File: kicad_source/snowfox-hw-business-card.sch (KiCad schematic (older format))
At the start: 7 parts, among them CN2 CONN_01X18, CN3 CONN_01X18

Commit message: added flash, JTAG connector and display to schematic
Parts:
- removed CN2, CN3: CONN_01X18, pin_headers:Pin_Header_Straight_1x18, symbol mechanical-connectors:CONN_01X18
- removed D1: 150060YS75000, LEDs:LED_0603, symbol devices:Led_Small
- removed R1: 3k3, resistors:R_0603, symbol devices:R_0603
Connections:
- net labels removed: +3V3, GND, PEX_PIN1, PEX_PIN10, PEX_PIN11, PEX_PIN12, PEX_PIN13, PEX_PIN14, PEX_PIN16, PEX_PIN20, PEX_PIN23, PEX_PIN25, PEX_PIN28, PEX_PIN3, PEX_PIN30, PEX_PIN31, PEX_PIN32, PEX_PIN33, PEX_PIN42, PEX_PIN44, PEX_PIN45, PEX_PIN46, PEX_PIN47, PEX_PIN48, PEX_PIN49, PEX_PIN5, PEX_PIN51, PEX_PIN6, PEX_PIN7, PEX_PIN8, PEX_RST, WM_PIO24, WM_PIO25
- wire segments 45 -> 0

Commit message: added nfc part, generated schematic pdf
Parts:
- renumbered MECH3 to MECH1, MECH4 to MECH2, MECH5 to MECH3
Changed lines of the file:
@@
 $Descr A4 11693 8268
 encoding utf-8
-Sheet 1 6
+Sheet 1 7
 Title "snowfox-hw-business-card"
-Date "2020-05-07"
+Date "2020-05-10"
 Rev "dev_0.1"
 Comp "generationmake"
@@
 $EndDescr
 $Comp
-L MECH_mounting-holes:MHP_3.2_5.8 MECH3
+L MECH_mounting-holes:MHP_3.2_5.8 MECH1
 U 1 1 5E401602
 P 1000 7600
-F 0 "MECH3" H 1128 7646 50  0000 L CNN
+F 0 "MECH1" H 1128 7646 50  0000 L CNN
 F 1 "MHP_3.2_5.8" H 1128 7555 50  0000 L CNN
 F 2 "MECH_mounting_holes:MHP_3.2_5.8" H 900 7650 50  0001 C CNN
@@
 $EndComp
 $Comp
-L MECH_mounting-holes:MHP_3.2_5.8 MECH4
+L MECH_mounting-holes:MHP_3.2_5.8 MECH2
 U 1 1 5E401D77
 P 2000 7600
-F 0 "MECH4" H 2128 7646 50  0000 L CNN
+F 0 "MECH2" H 2128 7646 50  0000 L CNN
 F 1 "MHP_3.2_5.8" H 2128 7555 50  0000 L CNN
 F 2 "MECH_mounting_holes:MHP_3.2_5.8" H 1900 7650 50  0001 C CNN
@@
 $EndComp
 $Comp
-L MECH_mounting-holes:MHP_3.2_5.8 MECH5
+L MECH_mounting-holes:MHP_3.2_5.8 MECH3
 U 1 1 5E402150
 P 3000 7600
-F 0 "MECH5" H 3128 7646 50  0000 L CNN
+F 0 "MECH3" H 3128 7646 50  0000 L CNN
 F 1 "MHP_3.2_5.8" H 3128 7555 50  0000 L CNN
 F 2 "MECH_mounting_holes:MHP_3.2_5.8" H 2900 7650 50  0001 C CNN
@@
 F1 "history.sch" 43
 $EndSheet
+$Sheet
+S 3000 2000 1000 500
+U 5EB7BA95
+F0 "NFC" 43
+F1 "nfc.sch" 43
+$EndSheet
 $EndSCHEMATC

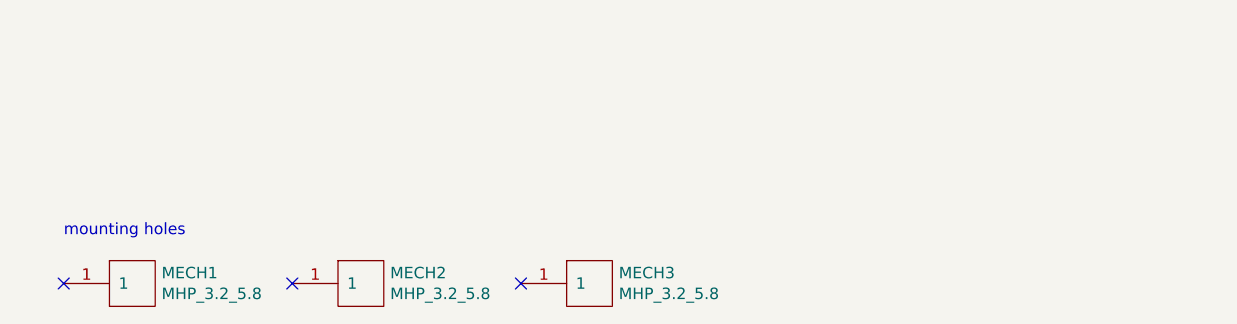
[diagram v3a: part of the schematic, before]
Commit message: used small side switch for reset, added expansion connector,changed mounting holes
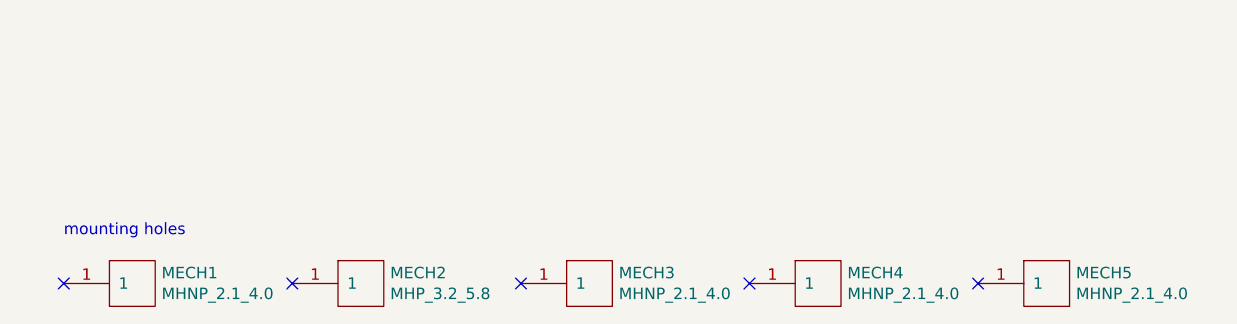
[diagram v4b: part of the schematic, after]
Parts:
- removed MECH1, MECH3: MHP_3.2_5.8, MECH_mounting_holes:MHP_3.2_5.8, symbol MECH_mounting-holes:MHP_3.2_5.8
- added MECH1, MECH3, MECH4, MECH5: MHNP_2.1_4.0, MECH_mounting_holes:MH_210_400_NP, symbol MECH_mounting-holes:MHNP_2.1_4.0
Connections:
- no-connect marks 3 -> 5
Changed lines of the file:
@@
 Comment4 ""
 $EndDescr
-$Comp
-L MECH_mounting-holes:MHP_3.2_5.8 MECH1
-U 1 1 5E401602
-P 1000 7600
-F 0 "MECH1" H 1128 7646 50  0000 L CNN
-F 1 "MHP_3.2_5.8" H 1128 7555 50  0000 L CNN
-F 2 "MECH_mounting_holes:MHP_3.2_5.8" H 900 7650 50  0001 C CNN
-F 3 "" H 1000 7600 50  0001 C CNN
-	1    1000 7600
-	1    0    0    -1
-$EndComp
-$Comp
-L MECH_mounting-holes:MHP_3.2_5.8 MECH2
-U 1 1 5E401D77
-P 2000 7600
-F 0 "MECH2" H 2128 7646 50  0000 L CNN
-F 1 "MHP_3.2_5.8" H 2128 7555 50  0000 L CNN
-F 2 "MECH_mounting_holes:MHP_3.2_5.8" H 1900 7650 50  0001 C CNN
-F 3 "" H 2000 7600 50  0001 C CNN
-	1    2000 7600
-	1    0    0    -1
-$EndComp
-$Comp
-L MECH_mounting-holes:MHP_3.2_5.8 MECH3
-U 1 1 5E402150
-P 3000 7600
-F 0 "MECH3" H 3128 7646 50  0000 L CNN
-F 1 "MHP_3.2_5.8" H 3128 7555 50  0000 L CNN
-F 2 "MECH_mounting_holes:MHP_3.2_5.8" H 2900 7650 50  0001 C CNN
-F 3 "" H 3000 7600 50  0001 C CNN
-	1    3000 7600
-	1    0    0    -1
-$EndComp
-NoConn ~ 2700 7600
 NoConn ~ 1700 7600
 NoConn ~ 700  7600
@@
 F1 "nfc.sch" 43
 $EndSheet
+$Comp
+L MECH_mounting-holes:MHP_3.2_5.8 MECH2
+U 1 1 5ED84539
+P 2000 7600
+F 0 "MECH2" H 2128 7646 50  0000 L CNN
+F 1 "MHP_3.2_5.8" H 2128 7555 50  0000 L CNN
+F 2 "MECH_mounting_holes:MHP_3.2_5.8" H 1900 7650 50  0001 C CNN
+F 3 "" H 2000 7600 50  0001 C CNN
+	1    2000 7600
+	1    0    0    -1
+$EndComp
+$Comp
+L MECH_mounting-holes:MHNP_2.1_4.0 MECH1
+U 1 1 5ED847C4
+P 1000 7600
+F 0 "MECH1" H 1128 7646 50  0000 L CNN
+F 1 "MHNP_2.1_4.0" H 1128 7555 50  0000 L CNN
+F 2 "MECH_mounting_holes:MH_210_400_NP" H 900 7650 50  0001 C CNN
+F 3 "" H 1000 7600 50  0001 C CNN
+	1    1000 7600
+	1    0    0    -1
+$EndComp
+NoConn ~ 2700 7600
+$Comp
+L MECH_mounting-holes:MHNP_2.1_4.0 MECH3
+U 1 1 5ED84C02
+P 3000 7600
+F 0 "MECH3" H 3128 7646 50  0000 L CNN
+F 1 "MHNP_2.1_4.0" H 3128 7555 50  0000 L CNN
+F 2 "MECH_mounting_holes:MH_210_400_NP" H 2900 7650 50  0001 C CNN
+F 3 "" H 3000 7600 50  0001 C CNN
+	1    3000 7600
+	1    0    0    -1
+$EndComp
+NoConn ~ 3700 7600
+$Comp
+L MECH_mounting-holes:MHNP_2.1_4.0 MECH4
+U 1 1 5ED85171
+P 4000 7600
+F 0 "MECH4" H 4128 7646 50  0000 L CNN
+F 1 "MHNP_2.1_4.0" H 4128 7555 50  0000 L CNN
+F 2 "MECH_mounting_holes:MH_210_400_NP" H 3900 7650 50  0001 C CNN
+F 3 "" H 4000 7600 50  0001 C CNN
+	1    4000 7600
+	1    0    0    -1
+$EndComp
+NoConn ~ 4700 7600
+$Comp
+L MECH_mounting-holes:MHNP_2.1_4.0 MECH5
+U 1 1 5ED85C08
+P 5000 7600
+F 0 "MECH5" H 5128 7646 50  0000 L CNN
+F 1 "MHNP_2.1_4.0" H 5128 7555 50  0000 L CNN
+F 2 "MECH_mounting_holes:MH_210_400_NP" H 4900 7650 50  0001 C CNN
+F 3 "" H 5000 7600 50  0001 C CNN
+	1    5000 7600
+	1    0    0    -1
+$EndComp
 $EndSCHEMATC

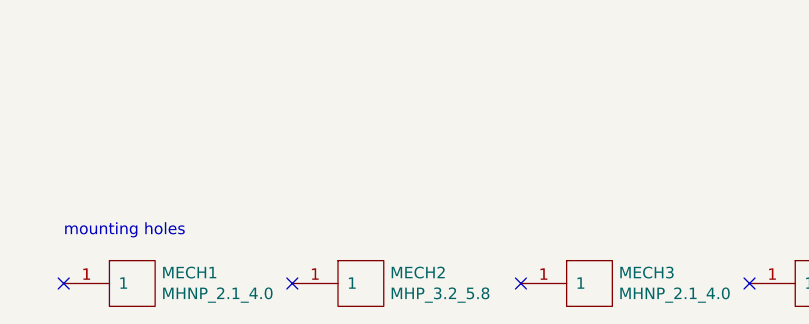
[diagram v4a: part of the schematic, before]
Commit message: rearranged parts for display
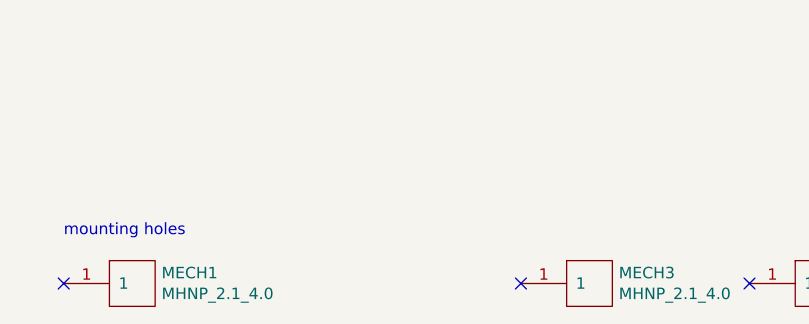
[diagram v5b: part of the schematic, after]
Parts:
- removed MECH2: MHP_3.2_5.8, MECH_mounting_holes:MHP_3.2_5.8, symbol MECH_mounting-holes:MHP_3.2_5.8
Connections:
- no-connect marks 5 -> 4
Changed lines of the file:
@@
 Comment4 ""
 $EndDescr
-NoConn ~ 1700 7600
 NoConn ~ 700  7600
 Text Notes 700  7400 0    50   ~ 0
@@
 $EndSheet
 $Comp
-L MECH_mounting-holes:MHP_3.2_5.8 MECH2
-U 1 1 5ED84539
-P 2000 7600
-F 0 "MECH2" H 2128 7646 50  0000 L CNN
-F 1 "MHP_3.2_5.8" H 2128 7555 50  0000 L CNN
-F 2 "MECH_mounting_holes:MHP_3.2_5.8" H 1900 7650 50  0001 C CNN
-F 3 "" H 2000 7600 50  0001 C CNN
-	1    2000 7600
-	1    0    0    -1
-$EndComp
-$Comp
 L MECH_mounting-holes:MHNP_2.1_4.0 MECH1

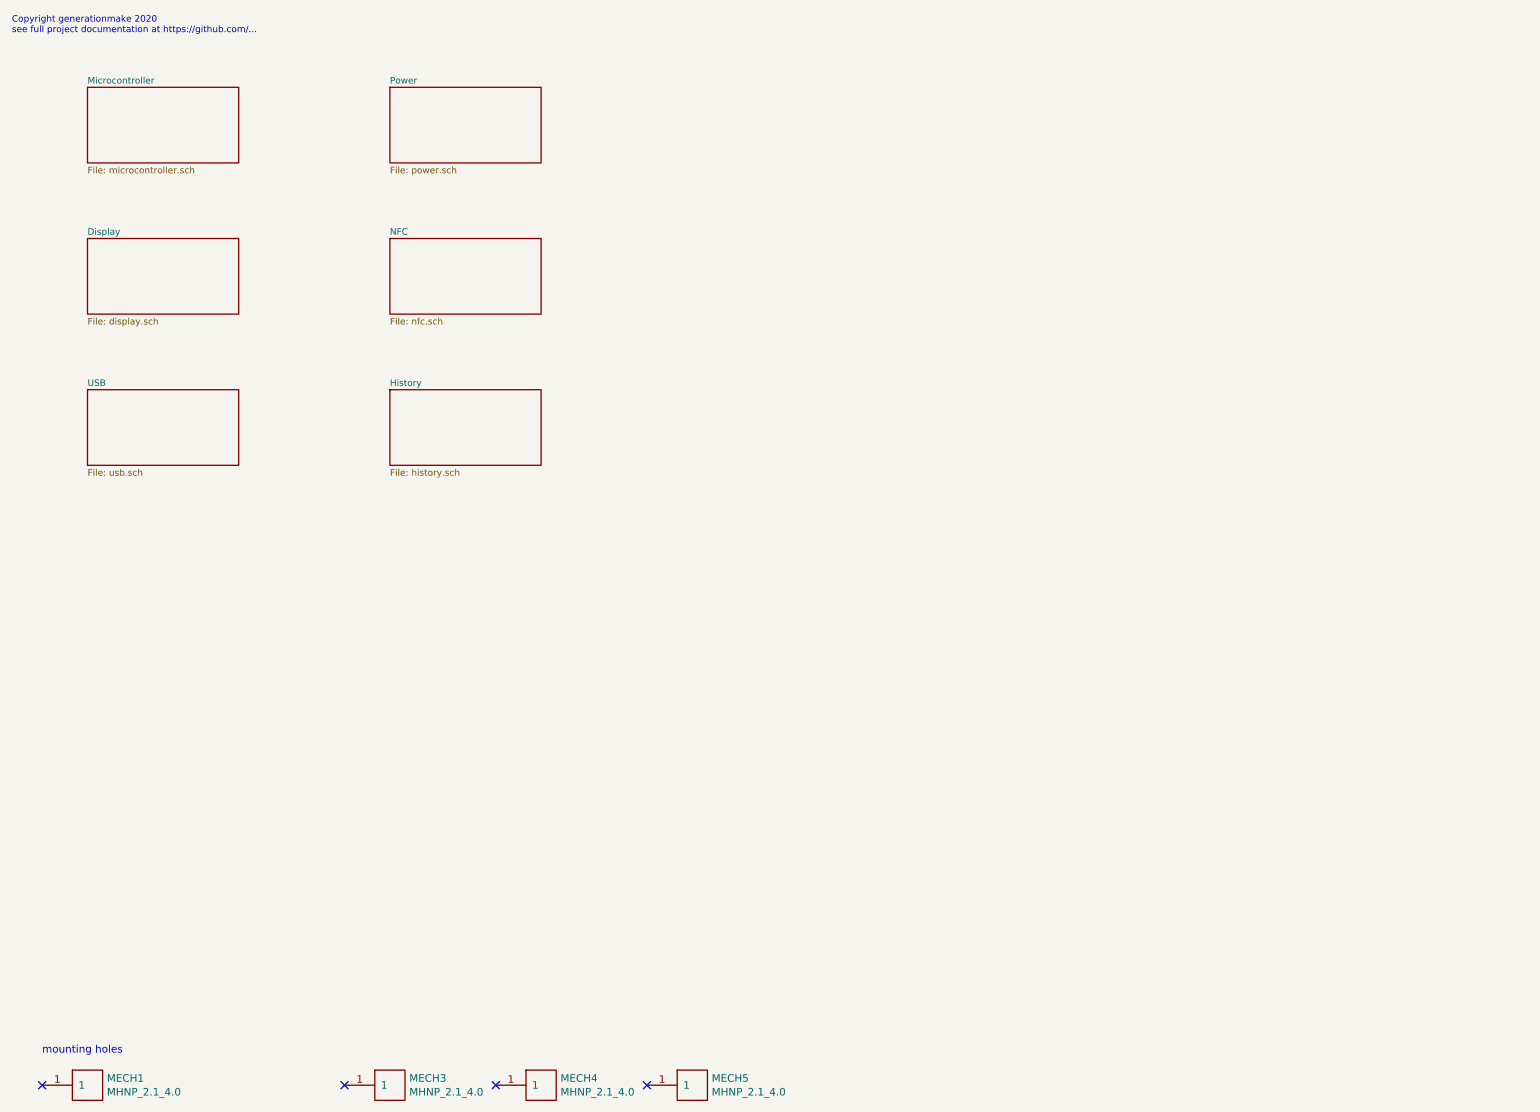
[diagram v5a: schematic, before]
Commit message: added C45 to pin4 of display
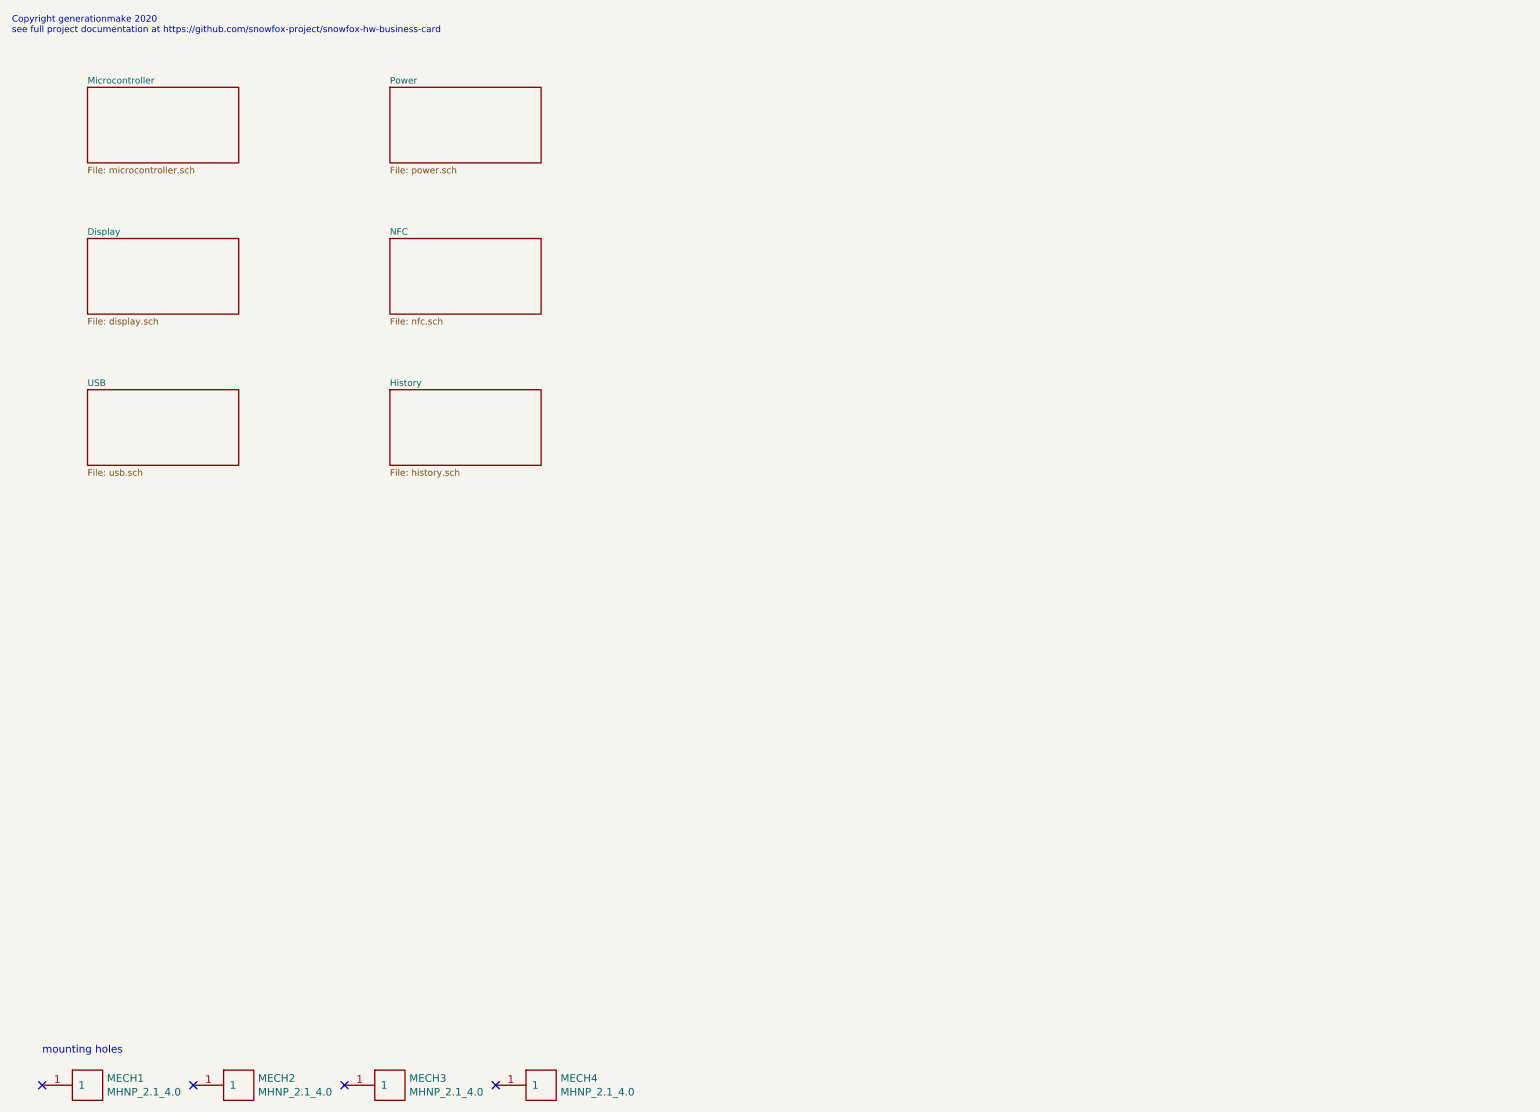
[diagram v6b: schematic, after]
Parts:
- renumbered MECH3 to MECH2, MECH4 to MECH3, MECH5 to MECH4
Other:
- note added: "Copyright generationmake 2020\nsee full project documentation at https://github.com/snowfox-project/snowfox-hw-business-card"
- note removed: "Copyright generationmake 2020\nsee full project documentation at https://github.com/..."
- moved on the sheet: MECH2, MECH3, MECH4
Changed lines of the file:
@@
 Sheet 1 7
 Title "snowfox-hw-business-card"
-Date "2020-05-13"
+Date "2020-07-03"
 Rev "dev_0.1"
 Comp "generationmake"
@@
 mounting holes
 Text Notes 500  650  0    43   ~ 0
-Copyright generationmake 2020\nsee full project documentation at https://github.com/...
+Copyright generationmake 2020\nsee full project documentation at https://github.com/snowfox-project/snowfox-hw-business-card
 $Sheet
 S 1000 1000 1000 500
@@
 $EndSheet
 $Sheet
+S 3000 2000 1000 500
+U 5EB7BA95
+F0 "NFC" 43
+F1 "nfc.sch" 43
+$EndSheet
+$Sheet
 S 3000 3000 1000 500
 U 5EB369DF
 F0 "History" 43
 F1 "history.sch" 43
-$EndSheet
-$Sheet
-S 3000 2000 1000 500
-U 5EB7BA95
-F0 "NFC" 43
-F1 "nfc.sch" 43
 $EndSheet
 $Comp
@@
 	1    0    0    -1
 $EndComp
+NoConn ~ 1700 7600
+$Comp
+L MECH_mounting-holes:MHNP_2.1_4.0 MECH2
+U 1 1 5ED84C02
+P 2000 7600
+F 0 "MECH2" H 2128 7646 50  0000 L CNN
+F 1 "MHNP_2.1_4.0" H 2128 7555 50  0000 L CNN
+F 2 "MECH_mounting_holes:MH_210_400_NP" H 1900 7650 50  0001 C CNN
+F 3 "" H 2000 7600 50  0001 C CNN
+	1    2000 7600
+	1    0    0    -1
+$EndComp
 NoConn ~ 2700 7600
 $Comp
 L MECH_mounting-holes:MHNP_2.1_4.0 MECH3
-U 1 1 5ED84C02
+U 1 1 5ED85171
 P 3000 7600
 F 0 "MECH3" H 3128 7646 50  0000 L CNN
@@
 $Comp
 L MECH_mounting-holes:MHNP_2.1_4.0 MECH4
-U 1 1 5ED85171
+U 1 1 5ED85C08
 P 4000 7600
 F 0 "MECH4" H 4128 7646 50  0000 L CNN
@@
 	1    0    0    -1
 $EndComp
-NoConn ~ 4700 7600
-$Comp
-L MECH_mounting-holes:MHNP_2.1_4.0 MECH5
-U 1 1 5ED85C08
-P 5000 7600
-F 0 "MECH5" H 5128 7646 50  0000 L CNN
-F 1 "MHNP_2.1_4.0" H 5128 7555 50  0000 L CNN
-F 2 "MECH_mounting_holes:MH_210_400_NP" H 4900 7650 50  0001 C CNN
-F 3 "" H 5000 7600 50  0001 C CNN
-	1    5000 7600
-	1    0    0    -1
-$EndComp
